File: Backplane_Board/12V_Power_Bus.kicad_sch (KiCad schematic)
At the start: 17 parts, among them U4 PKJ7213WPI

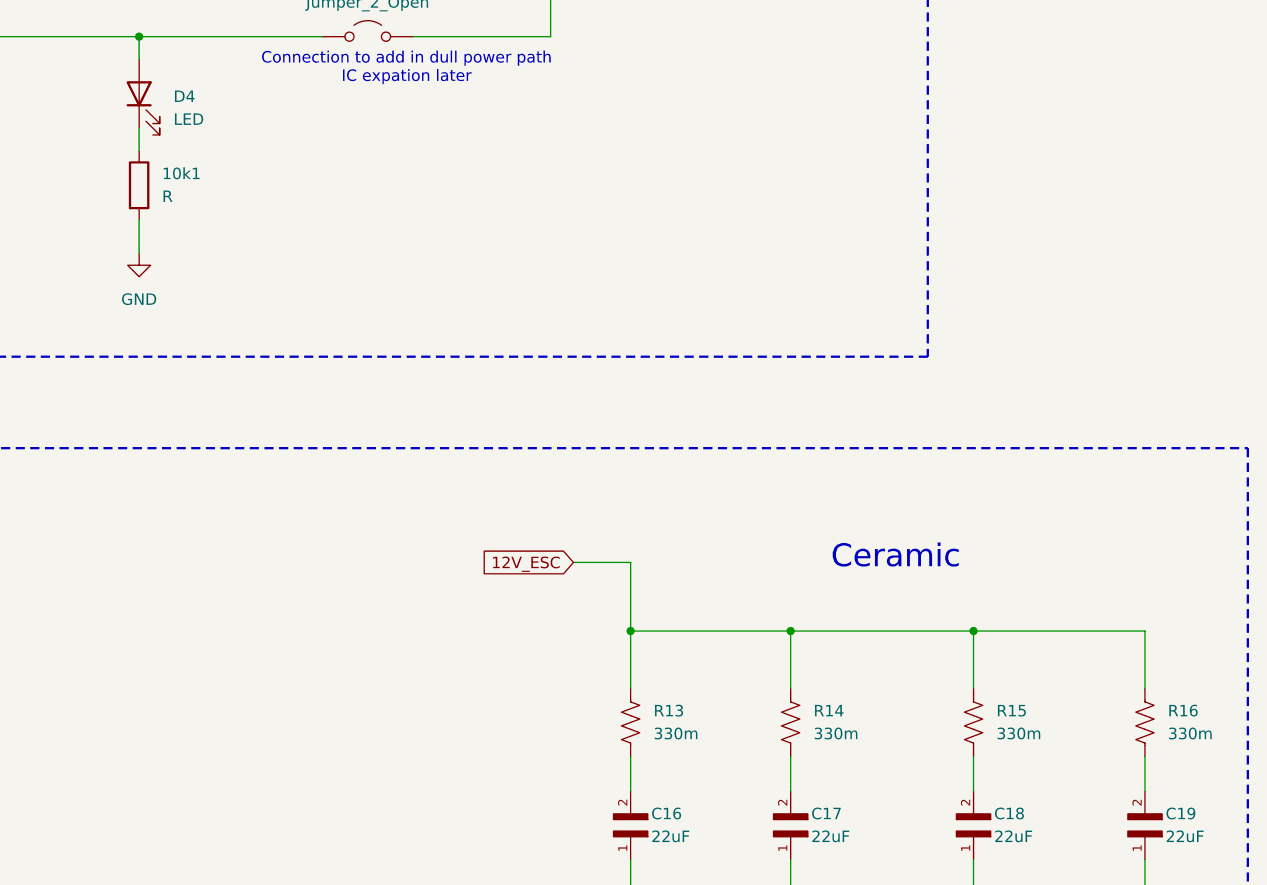
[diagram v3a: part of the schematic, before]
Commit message: adding more footprints
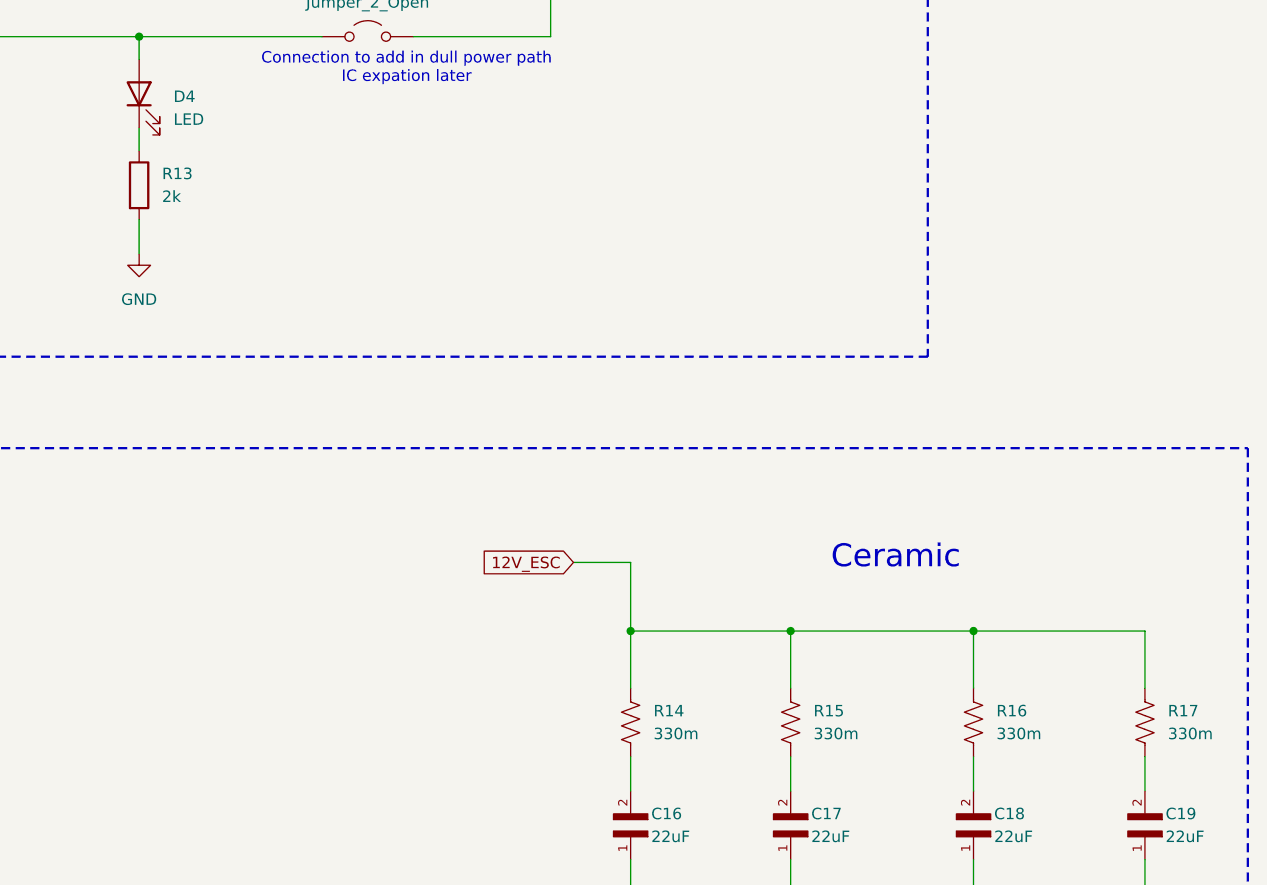
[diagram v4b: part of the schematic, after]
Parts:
- C14, C15: footprint (none) -> Capacitor_THT:CP_Radial_D13.0mm_P5.00mm
- D4: footprint (none) -> LED_SMD:LED_0603_1608Metric
- JP5: footprint (none) -> Connector_AMASS:AMASS_XT60-F_1x02_P7.20mm_Vertical
- R11, R12: footprint (none) -> Inductor_SMD:L_1206_3216Metric
- R13: renamed from 10k1; value R -> 2k; footprint (none) -> Resistor_SMD:R_1206_3216Metric_Pad1.30x1.75mm_HandSolder
- renumbered R13 to R14, R14 to R15, R15 to R16, R16 to R17
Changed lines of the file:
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@@
+					(unit 1)
+				)
+				(path "/4484cfee-9e43-4cef-88b4-a8ca308542b4/829c4f27-479c-4774-bd79-d7d13a3cb460"
+					(reference "C13")
 					(unit 1)
 				)
@@
 			)
 		)
-		(property "Footprint" ""
+		(property "Footprint" "Capacitor_THT:CP_Radial_D13.0mm_P5.00mm"
 			(at 95.25 127 0)
 			(effects
@@
 		(dnp no)
 		(fields_autoplaced yes)
-		(property "Reference" "10k1"
+		(property "Reference" "R13"
 			(at 137.16 64.7699 0)
 			(effects
@@
 			)
 		)
-		(property "Value" "R"
+		(property "Value" "2k"
 			(at 137.16 67.3099 0)
 			(effects
@@
 			)
 		)
-		(property "Footprint" ""
+		(property "Footprint" "Resistor_SMD:R_1206_3216Metric_Pad1.30x1.75mm_HandSolder"
 			(at 132.842 66.04 90)
 			(effects
@@
 			(project "Backplane_Board"
 				(path "/4484cfee-9e43-4cef-88b4-a8ca308542b4/7cc9cec9-7faa-4853-bd66-b7a2d884c738"
-					(reference "10k1")
+					(reference "R13")
 					(unit 1)
 				)
@@
 			)
 		)
-		(property "Footprint" ""
+		(property "Footprint" "Connector_AMASS:AMASS_XT60-F_1x02_P7.20mm_Vertical"
 			(at 160.02 49.53 0)
 			(effects
@@
 			)
 		)
-		(property "Footprint" ""
+		(property "Footprint" "Capacitor_THT:CP_Radial_D13.0mm_P5.00mm"
 			(at 83.82 127 0)
 			(effects
@@
 		(dnp no)
 		(fields_autoplaced yes)
-		(property "Reference" "R13"
+		(property "Reference" "R14"
 			(at 191.77 124.4599 0)
 			(effects
@@
 			(project "Backplane_Board"
 				(path "/4484cfee-9e43-4cef-88b4-a8ca308542b4/7cc9cec9-7faa-4853-bd66-b7a2d884c738"
-					(reference "R13")
+					(reference "R14")
 					(unit 1)
 				)
@@
 			)
 		)
-		(property "Footprint" ""
+		(property "Footprint" "LED_SMD:LED_0603_1608Metric"
 			(at 134.62 55.88 0)
 			(effects
@@
 			)
 		)
-		(property "Footprint" ""
+		(property "Footprint" "Inductor_SMD:L_1206_3216Metric"
 			(at 103.632 43.18 90)
 			(effects
@@
 		(dnp no)
 		(fields_autoplaced yes)
-		(property "Reference" "R15"
+		(property "Reference" "R16"
 			(at 229.87 124.4599 0)
 			(effects
@@
 			(project "Backplane_Board"
 				(path "/4484cfee-9e43-4cef-88b4-a8ca308542b4/7cc9cec9-7faa-4853-bd66-b7a2d884c738"
-					(reference "R15")
+					(reference "R16")
 					(unit 1)
 				)
@@
 		(dnp no)
 		(fields_autoplaced yes)
-		(property "Reference" "R16"
+		(property "Reference" "R17"
 			(at 248.92 124.4599 0)
 			(effects
@@
 			(project "Backplane_Board"
 				(path "/4484cfee-9e43-4cef-88b4-a8ca308542b4/7cc9cec9-7faa-4853-bd66-b7a2d884c738"
-					(reference "R16")
+					(reference "R17")
 					(unit 1)
 				)
@@
 			)
 		)
-		(property "Footprint" ""
+		(property "Footprint" "Inductor_SMD:L_1206_3216Metric"
 			(at 103.632 31.75 90)
 			(effects
@@
 		(dnp no)
 		(fields_autoplaced yes)
-		(property "Reference" "R14"
+		(property "Reference" "R15"
 			(at 209.55 124.4599 0)
 			(effects
@@
 			(project "Backplane_Board"
 				(path "/4484cfee-9e43-4cef-88b4-a8ca308542b4/7cc9cec9-7faa-4853-bd66-b7a2d884c738"
-					(reference "R14")
-					(unit 1)
-				)
+					(reference "R15")
+					(unit 1)
+				)

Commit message: derat nest ifcation
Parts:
- removed C15: 680u, Capacitor_THT:CP_Radial_D13.0mm_P5.00mm, symbol Device:C_Polarized_Small_US
- removed JP5: Jumper_2_Open, Connector_AMASS:AMASS_XT60-F_1x02_P7.20mm_Vertical, symbol Jumper:Jumper_2_Open
- C13: footprint (none) -> Capacitor_THT:CP_Radial_D13.0mm_P5.00mm
- C15: renamed from C16; footprint C2012X5R1V226M125AC:CAPC2012X145N -> Capacitor_SMD:C_1206_3216Metric_Pad1.33x1.80mm_HandSolder
- C16: renamed from C17; footprint C2012X5R1V226M125AC:CAPC2012X145N -> Capacitor_SMD:C_1206_3216Metric_Pad1.33x1.80mm_HandSolder
- C17: renamed from C18; footprint C2012X5R1V226M125AC:CAPC2012X145N -> Capacitor_SMD:C_1206_3216Metric_Pad1.33x1.80mm_HandSolder
- C18: renamed from C19; footprint C2012X5R1V226M125AC:CAPC2012X145N -> Capacitor_SMD:C_1206_3216Metric_Pad1.33x1.80mm_HandSolder
- R13: footprint Resistor_SMD:R_1206_3216Metric_Pad1.30x1.75mm_HandSolder -> Resistor_SMD:R_0805_2012Metric_Pad1.20x1.40mm_HandSolder
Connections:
- net +12V: now also D4.2 (A), R12.2, U4.8 (+Sense), U4.9 (+Out)
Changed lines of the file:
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@@
-	)
-	(junction
-		(at 83.82 134.62)
-		(diameter 0)
-		(color 0 0 0 0)
 	)
 	(junction
@@
 	)
 	(junction
-		(at 83.82 119.38)
-		(diameter 0)
-		(color 0 0 0 0)
-	)
-	(junction
 		(at 105.41 49.53)
 		(diameter 0)
@@
 	(wire
 		(pts
-			(xy 134.62 49.53) (xy 154.94 49.53)
+			(xy 134.62 49.53) (xy 180.34 49.53)
 		)
 		(stroke
@@
 	(wire
 		(pts
-			(xy 83.82 119.38) (xy 95.25 119.38)
-		)
-		(stroke
-			(width 0)
-			(type default)
-		)
-	)
-	(wire
-		(pts
 			(xy 189.23 107.95) (xy 189.23 115.57)
 		)
@@
 	(wire
 		(pts
-			(xy 83.82 134.62) (xy 95.25 134.62)
-		)
-		(stroke
-			(width 0)
-			(type default)
-		)
-	)
-	(wire
-		(pts
 			(xy 207.01 115.57) (xy 227.33 115.57)
 		)
@@
 	(wire
 		(pts
-			(xy 165.1 49.53) (xy 180.34 49.53)
-		)
-		(stroke
-			(width 0)
-			(type default)
-		)
-	)
-	(wire
-		(pts
 			(xy 95.25 45.72) (xy 95.25 49.53)
 		)
@@
 	(wire
 		(pts
-			(xy 95.25 119.38) (xy 95.25 124.46)
-		)
-		(stroke
-			(width 0)
-			(type default)
-		)
-	)
-	(wire
-		(pts
 			(xy 246.38 140.97) (xy 246.38 144.78)
 		)
@@
 		(pts
 			(xy 39.37 29.21) (xy 46.99 29.21)
-		)
-		(stroke
-			(width 0)
-			(type default)
-		)
-	)
-	(wire
-		(pts
-			(xy 95.25 129.54) (xy 95.25 134.62)
 		)
 		(stroke
@@
 			)
 		)
-		(property "Footprint" ""
+		(property "Footprint" "Capacitor_THT:CP_Radial_D13.0mm_P5.00mm"
 			(at 71.12 127 0)
 			(effects
@@
 				(path "/4484cfee-9e43-4cef-88b4-a8ca308542b4/829c4f27-479c-4774-bd79-d7d13a3cb460"
 					(reference "C13")
-					(unit 1)
-				)
-			)
-		)
-	)
-	(symbol
-		(lib_id "Device:C_Polarized_Small_US")
-		(at 95.25 127 0)
-		(unit 1)
-		(exclude_from_sim no)
-		(in_bom yes)
-		(on_board yes)
-		(dnp no)
-		(fields_autoplaced yes)
-		(property "Reference" "C15"
-			(at 97.79 125.2981 0)
-			(effects
-				(font
-					(size 1.27 1.27)
-				)
-				(justify left)
-			)
-		)
-		(property "Value" "680u"
-			(at 97.79 127.8381 0)
-			(effects
-				(font
-					(size 1.27 1.27)
-				)
-				(justify left)
-			)
-		)
-		(property "Footprint" "Capacitor_THT:CP_Radial_D13.0mm_P5.00mm"
-			(at 95.25 127 0)
-			(effects
-				(font
-					(size 1.27 1.27)
-				)
-				(hide yes)
-			)
-		)
-		(property "Datasheet" "https://www.digikey.com/en/products/detail/kemet/A750MW687M1VAAE018/13420117?s"
-			(at 95.25 127 0)
-			(effects
-				(font
-					(size 1.27 1.27)
-				)
-				(hide yes)
-			)
-		)
-		(property "Description" "A750MW687M1VAAE018"
-			(at 95.25 127 0)
-			(effects
-				(font
-					(size 1.27 1.27)
-				)
-				(hide yes)
-			)
-		)
-		(pin "1"
-		)
-		(pin "2"
-		)
-		(instances
-			(project "Backplane_Board"
-				(path "/4484cfee-9e43-4cef-88b4-a8ca308542b4/7cc9cec9-7faa-4853-bd66-b7a2d884c738"
-					(reference "C15")
 					(unit 1)
 				)
@@
 			)
 		)
-		(property "Footprint" "Resistor_SMD:R_1206_3216Metric_Pad1.30x1.75mm_HandSolder"
+		(property "Footprint" "Resistor_SMD:R_0805_2012Metric_Pad1.20x1.40mm_HandSolder"
 			(at 132.842 66.04 90)
 			(effects
@@
 	)
 	(symbol
-		(lib_id "Jumper:Jumper_2_Open")
-		(at 160.02 49.53 0)
-		(unit 1)
-		(exclude_from_sim yes)
-		(in_bom yes)
-		(on_board yes)
-		(dnp no)
-		(fields_autoplaced yes)
-		(property "Reference" "JP5"
-			(at 160.02 43.18 0)
-			(effects
-				(font
-					(size 1.27 1.27)
-				)
-			)
-		)
-		(property "Value" "Jumper_2_Open"
-			(at 160.02 45.72 0)
-			(effects
-				(font
-					(size 1.27 1.27)
-				)
-			)
-		)
-		(property "Footprint" "Connector_AMASS:AMASS_XT60-F_1x02_P7.20mm_Vertical"
-			(at 160.02 49.53 0)
-			(effects
-				(font
-					(size 1.27 1.27)
-				)
-				(hide yes)
-			)
-		)
-		(property "Datasheet" "~"
-			(at 160.02 49.53 0)
-			(effects
-				(font
-					(size 1.27 1.27)
-				)
-				(hide yes)
-			)
-		)
-		(property "Description" "Jumper, 2-pole, open"
-			(at 160.02 49.53 0)
-			(effects
-				(font
-					(size 1.27 1.27)
-				)
-				(hide yes)
-			)
-		)
-		(pin "1"
-		)
-		(pin "2"
-		)
-		(instances
-			(project "Backplane_Board"
-				(path "/4484cfee-9e43-4cef-88b4-a8ca308542b4/7cc9cec9-7faa-4853-bd66-b7a2d884c738"
-					(reference "JP5")
-					(unit 1)
-				)
-			)
-		)
-	)
-	(symbol
 		(lib_id "power:GND")
 		(at 71.12 135.89 0)
@@
 		(on_board yes)
 		(dnp no)
-		(property "Reference" "C19"
+		(property "Reference" "C18"
 			(at 248.666 135.89 90)
 			(effects
@@
 			)
 		)
-		(property "Footprint" "C2012X5R1V226M125AC:CAPC2012X145N"
+		(property "Footprint" "Capacitor_SMD:C_1206_3216Metric_Pad1.33x1.80mm_HandSolder"
 			(at 246.38 138.43 0)
 			(effects
@@
 			(project "Backplane_Board"
 				(path "/4484cfee-9e43-4cef-88b4-a8ca308542b4/7cc9cec9-7faa-4853-bd66-b7a2d884c738"
-					(reference "C19")
+					(reference "C18")
 					(unit 1)
 				)
@@
 		(on_board yes)
 		(dnp no)
-		(property "Reference" "C17"
+		(property "Reference" "C16"
 			(at 209.296 135.89 90)
 			(effects
@@
 			)
 		)
-		(property "Footprint" "C2012X5R1V226M125AC:CAPC2012X145N"
+		(property "Footprint" "Capacitor_SMD:C_1206_3216Metric_Pad1.33x1.80mm_HandSolder"
 			(at 207.01 138.43 0)
 			(effects
@@
 			(project "Backplane_Board"
 				(path "/4484cfee-9e43-4cef-88b4-a8ca308542b4/7cc9cec9-7faa-4853-bd66-b7a2d884c738"
-					(reference "C17")
+					(reference "C16")
 					(unit 1)
 				)
@@
 		(on_board yes)
 		(dnp no)
-		(property "Reference" "C16"
+		(property "Reference" "C15"
 			(at 191.516 135.89 90)
 			(effects
@@
 			)
 		)
-		(property "Footprint" "C2012X5R1V226M125AC:CAPC2012X145N"
+		(property "Footprint" "Capacitor_SMD:C_1206_3216Metric_Pad1.33x1.80mm_HandSolder"
 			(at 189.23 138.43 0)
 			(effects
@@
 			(project "Backplane_Board"
 				(path "/4484cfee-9e43-4cef-88b4-a8ca308542b4/7cc9cec9-7faa-4853-bd66-b7a2d884c738"
-					(reference "C16")
+					(reference "C15")
 					(unit 1)
 				)
@@
 		(on_board yes)
 		(dnp no)
-		(property "Reference" "C18"
+		(property "Reference" "C17"
 			(at 229.616 135.89 90)
 			(effects
@@
 			)
 		)
-		(property "Footprint" "C2012X5R1V226M125AC:CAPC2012X145N"
+		(property "Footprint" "Capacitor_SMD:C_1206_3216Metric_Pad1.33x1.80mm_HandSolder"
 			(at 227.33 138.43 0)
 			(effects
@@
 			(project "Backplane_Board"
 				(path "/4484cfee-9e43-4cef-88b4-a8ca308542b4/7cc9cec9-7faa-4853-bd66-b7a2d884c738"
-					(reference "C18")
+					(reference "C17")
 					(unit 1)
 				)

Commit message: layout save
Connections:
- net 12V_ESC is gone; now on net +12V: C13.1, C14.1, R14.1, R15.1, R16.1, R17.1
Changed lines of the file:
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@@
-	(wire
-		(pts
-			(xy 182.88 107.95) (xy 189.23 107.95)
-		)
-		(stroke
-			(width 0)
-			(type default)
-		)
-	)
 	(wire
 		(pts
@@
 		(pts
 			(xy 92.71 19.05) (xy 92.71 26.67)
-		)
-		(stroke
-			(width 0)
-			(type default)
-		)
-	)
-	(wire
-		(pts
-			(xy 62.23 110.49) (xy 71.12 110.49)
 		)
 		(stroke
@@
 		)
 	)
-	(global_label "12V_ESC"
-		(shape input)
-		(at 182.88 107.95 180)
-		(fields_autoplaced yes)
-		(effects
-			(font
-				(size 1.27 1.27)
-			)
-			(justify right)
-		)
-		(property "Intersheetrefs" "${INTERSHEET_REFS}"
-			(at 171.7911 107.95 0)
-			(effects
-				(font
-					(size 1.27 1.27)
-				)
-				(justify right)
-				(hide yes)
-			)
-		)
-	)
-	(global_label "12V_ESC"
-		(shape input)
-		(at 62.23 110.49 180)
-		(fields_autoplaced yes)
-		(effects
-			(font
-				(size 1.27 1.27)
-			)
-			(justify right)
-		)
-		(property "Intersheetrefs" "${INTERSHEET_REFS}"
-			(at 51.1411 110.49 0)
-			(effects
-				(font
-					(size 1.27 1.27)
-				)
-				(justify right)
-				(hide yes)
-			)
-		)
-	)
 	(symbol
 		(lib_id "Device:C_Polarized_Small_US")
@@
 	)
 	(symbol
+		(lib_id "power:+12V")
+		(at 189.23 107.95 0)
+		(unit 1)
+		(exclude_from_sim no)
+		(in_bom yes)
+		(on_board yes)
+		(dnp no)
+		(fields_autoplaced yes)
+		(property "Reference" "#PWR083"
+			(at 189.23 111.76 0)
+			(effects
+				(font
+					(size 1.27 1.27)
+				)
+				(hide yes)
+			)
+		)
+		(property "Value" "+12V"
+			(at 189.23 102.87 0)
+			(effects
+				(font
+					(size 1.27 1.27)
+				)
+			)
+		)
+		(property "Footprint" ""
+			(at 189.23 107.95 0)
+			(effects
+				(font
+					(size 1.27 1.27)
+				)
+				(hide yes)
+			)
+		)
+		(property "Datasheet" ""
+			(at 189.23 107.95 0)
+			(effects
+				(font
+					(size 1.27 1.27)
+				)
+				(hide yes)
+			)
+		)
+		(property "Description" "Power symbol creates a global label with name \"+12V\""
+			(at 189.23 107.95 0)
+			(effects
+				(font
+					(size 1.27 1.27)
+				)
+				(hide yes)
+			)
+		)
+		(pin "1"
+		)
+		(instances
+			(project "Backplane_Board"
+				(path "/4484cfee-9e43-4cef-88b4-a8ca308542b4/7cc9cec9-7faa-4853-bd66-b7a2d884c738"
+					(reference "#PWR083")
+					(unit 1)
+				)
+			)
+		)
+	)
+	(symbol
 		(lib_id "power:GND")
 		(at 71.12 135.89 0)
@@
 					(unit 1)
 				)
+			)
+		)
+	)
+	(symbol
+		(lib_id "power:+12V")
+		(at 71.12 110.49 0)
+		(unit 1)
+		(exclude_from_sim no)
+		(in_bom yes)
+		(on_board yes)
+		(dnp no)
+		(fields_autoplaced yes)
+		(property "Reference" "#PWR082"
+			(at 71.12 114.3 0)
+			(effects
+				(font
+					(size 1.27 1.27)
+				)
+				(hide yes)
+			)
+		)
+		(property "Value" "+12V"
+			(at 71.12 105.41 0)
+			(effects
+				(font
+					(size 1.27 1.27)
+				)
+			)
+		)
+		(property "Footprint" ""
+			(at 71.12 110.49 0)
+			(effects
+				(font
+					(size 1.27 1.27)
+				)
+				(hide yes)
+			)
+		)
+		(property "Datasheet" ""
+			(at 71.12 110.49 0)
+			(effects
+				(font
+					(size 1.27 1.27)
+				)
+				(hide yes)
+			)
+		)
+		(property "Description" "Power symbol creates a global label with name \"+12V\""
+			(at 71.12 110.49 0)
+			(effects
+				(font
+					(size 1.27 1.27)
+				)
+				(hide yes)
+			)
+		)
+		(pin "1"
+		)
+		(instances
+			(project "Backplane_Board"
+				(path "/4484cfee-9e43-4cef-88b4-a8ca308542b4/7cc9cec9-7faa-4853-bd66-b7a2d884c738"
+					(reference "#PWR082")
+					(unit 1)
+				)

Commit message: added gerber
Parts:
- R13: value 2k -> 10k
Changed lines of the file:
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@@
 			)
 		)
-		(property "Value" "2k"
+		(property "Value" "10k"
 			(at 137.16 67.3099 0)
 			(effects
